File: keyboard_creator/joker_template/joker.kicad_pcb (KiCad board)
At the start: 2 copper layers, 80 x 60 mm, 20 parts, among them U1 BL24C256A-SFRC, U2 STM32F411CEU6, X1 ARM JTAG, Y1 7325-0800A2010-00

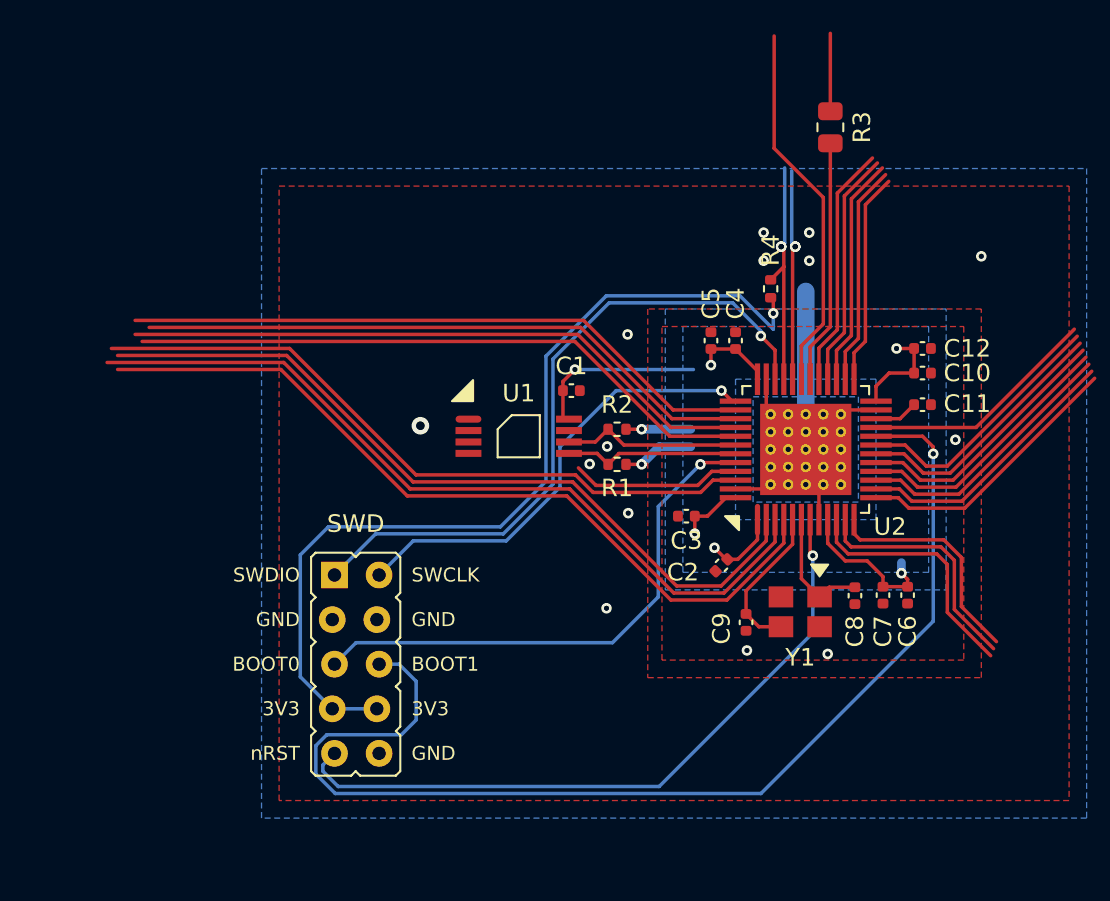
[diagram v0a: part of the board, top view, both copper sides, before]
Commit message: Update joker template to second revision
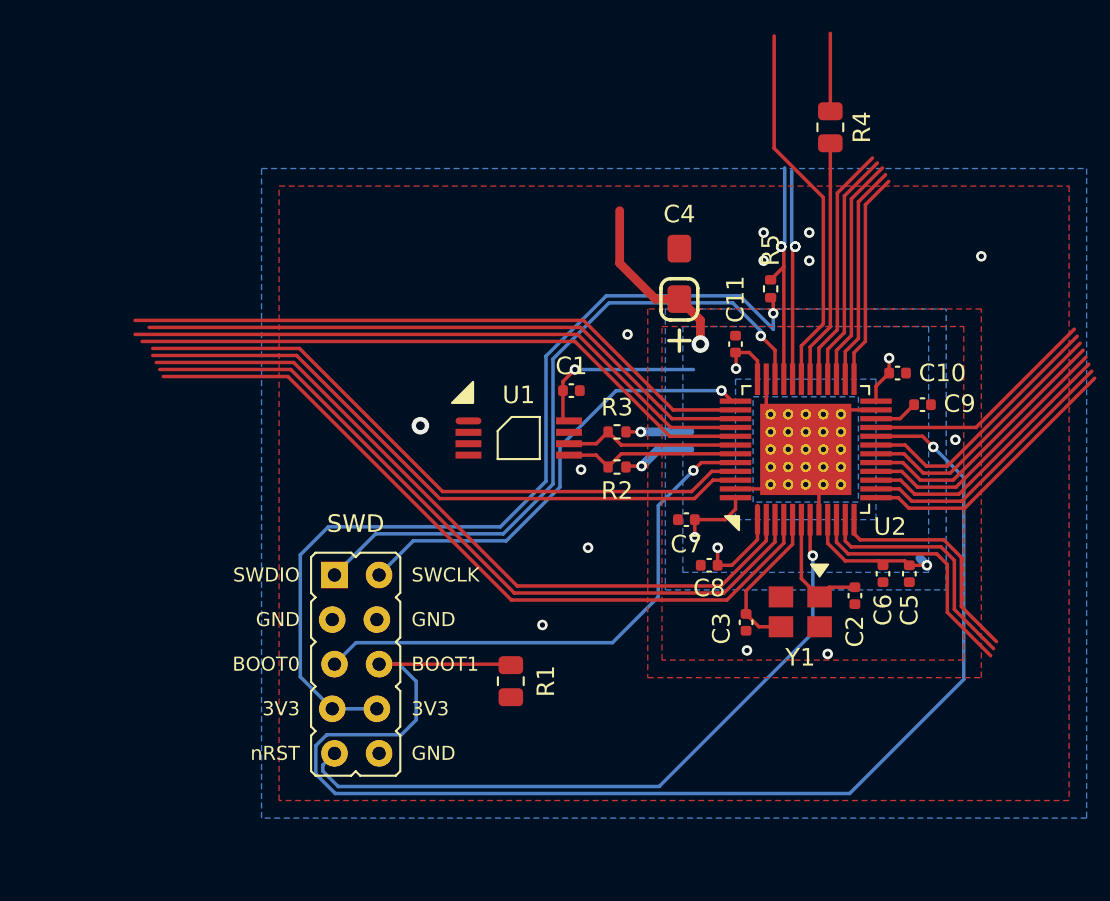
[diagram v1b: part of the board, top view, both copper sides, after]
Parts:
- removed C12: 4.7u, Capacitor_SMD:C_0402_1005Metric
- removed the C5 at (235.3, 118.9)
- added C4: 10u, acheron_Components:CP_EIA-3216-10_Kemet-I_Pad1.58x1.35mm_HandSolder, F.Cu at (233.5, 115.1)
- added R1: 10k, Resistor_SMD:R_0805_2012Metric, F.Cu at (223.9, 138.3)
- C9: renamed from C11; value 2.2u -> 4.7u
- moved C10 1.42 mm to (246.0, 120.8)
- moved C5 1.22 mm to (246.6, 132.2)
- moved C6 1.22 mm to (245.1, 132.2)
- moved C8 0.70 mm to (235.2, 131.7), turned to 180 degrees
- moved C7 0.20 mm to (233.9, 129.1)
- moved C11 0.20 mm to (236.7, 119.1)
- moved R2 0.15 mm to (230.0, 126.1)
- moved R3 0.15 mm to (230.0, 124.1)
- moved U1 0.10 mm to (224.4, 124.5)
- renumbered C4 to C11, C8 to C2, C9 to C3, C6 to C5, C7 to C6, C3 to C7, C2 to C8, R1 to R2, R2 to R3, R3 to R4, R4 to R5
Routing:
- net unconnected-(U2-Pad45): track 9.70 -> 37.1 mm
- net PB2/BOOT1: track 65.8 -> 77.7 mm
- net 3V3: track 96.5 -> 104.1 mm, vias 9 -> 10
- net GND: track 15.2 -> 8.23 mm, vias 14 -> 13
- net unconnected-(U2-Pad3): track 46.0 -> 42.8 mm
- net unconnected-(U2-Pad4): track 46.1 -> 43.3 mm
- net unconnected-(U2-Pad2): track 44.7 -> 42.3 mm
- net unconnected-(U2-Pad46): track 39.2 -> 37.0 mm

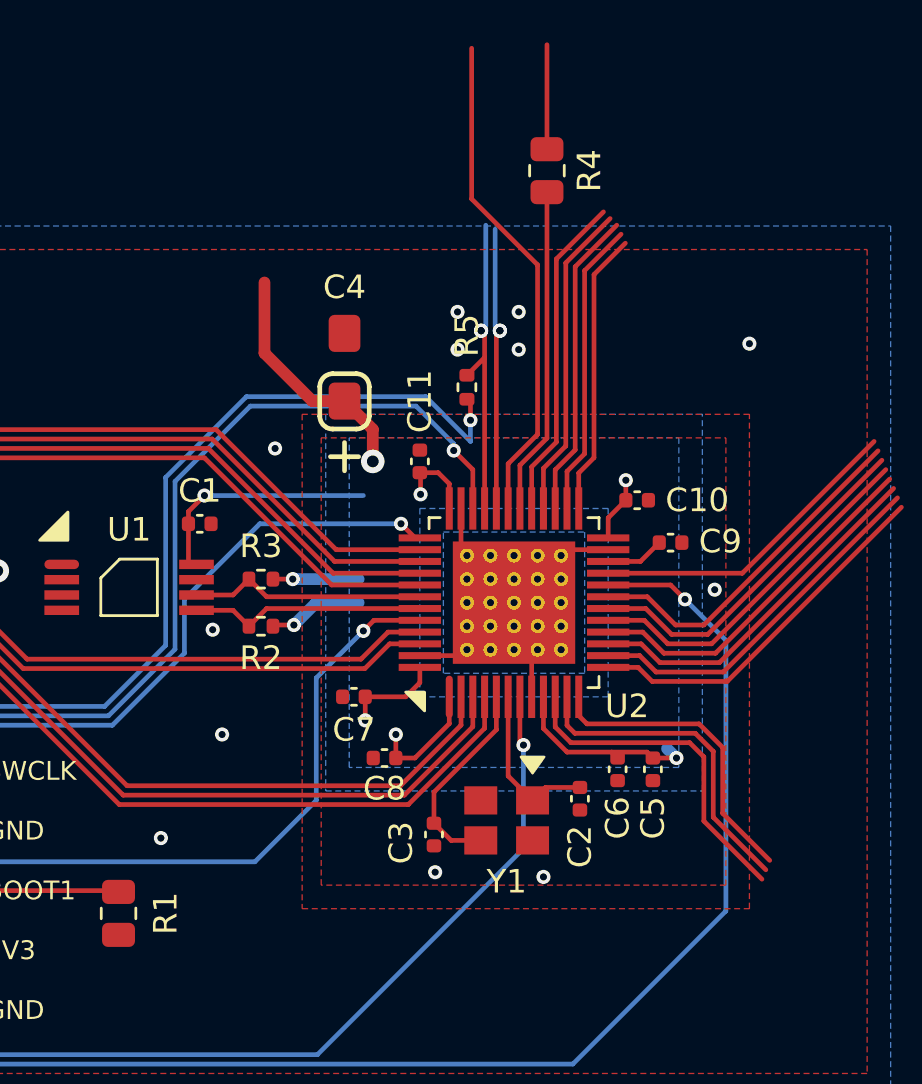
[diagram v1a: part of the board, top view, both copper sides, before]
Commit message: Added KiCAD Dockerfile for building kicad nightly
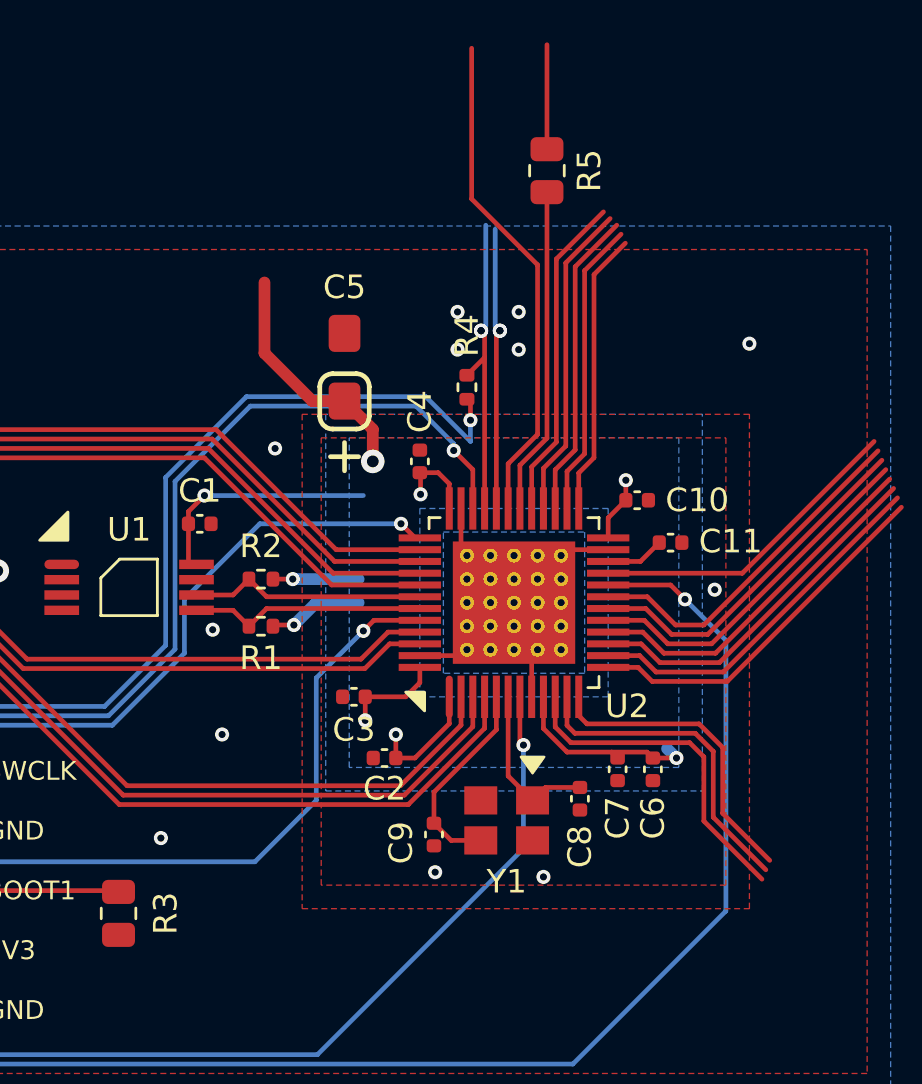
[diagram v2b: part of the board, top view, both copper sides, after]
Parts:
- renumbered C9 to C11, C8 to C2, C7 to C3, C11 to C4, C4 to C5, C5 to C6, C6 to C7, C2 to C8, C3 to C9, R2 to R1, R3 to R2, R1 to R3, R5 to R4, R4 to R5
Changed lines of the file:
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@@
   )
   (net 0 "")
-  (net 1 "Net-(C9-Pad2)")
+  (net 1 "Net-(C11-Pad2)")
   (net 2 "GND")
   (net 3 "3V3")
@@
     (property "Sheetname" "")
     (attr smd)
-    (fp_text reference "C3" (at 0.35 1.4 90) (layer "F.SilkS")
+    (fp_text reference "C9" (at 0.35 1.4 90) (layer "F.SilkS")
       (effects (font (size 1 1) (thickness 0.2)))
     )
@@
     (property "Sheetname" "")
     (attr smd)
-    (fp_text reference "C9" (at -1.2 0.05) (layer "F.SilkS")
+    (fp_text reference "C11" (at -1.2 0.05) (layer "F.SilkS")
       (effects (font (size 1 1) (thickness 0.2)) (justify left))
     )
@@
       (net 2 "GND") (pintype "passive"))
     (pad "2" smd roundrect locked (at 0.48 0 180) (size 0.56 0.62) (layers "F.Cu" "F.Paste" "F.Mask") (roundrect_rratio 0.25)
-      (net 1 "Net-(C9-Pad2)") (pintype "passive"))
+      (net 1 "Net-(C11-Pad2)") (pintype "passive"))
     (model "${KICAD6_3DMODEL_DIR}/Capacitor_SMD.3dshapes/C_0402_1005Metric.wrl"
       (offset (xyz 0 0 0))
@@
     (property "Sheetname" "")
     (attr smd)
-    (fp_text reference "R4" (at 0 -1.8 90) (layer "F.SilkS")
+    (fp_text reference "R5" (at 0 -1.8 90) (layer "F.SilkS")
       (effects (font (size 1 1) (thickness 0.2)))
     )
@@
       (net 26 "unconnected-(U2-Pad21)") (pinfunction "B10") (pintype "bidirectional"))
     (pad "22" smd rect locked (at 1.75 4 180) (size 1.8 0.3) (layers "F.Cu" "F.Paste" "F.Mask")
-      (net 1 "Net-(C9-Pad2)") (pinfunction "VCAP_1") (pintype "output"))
+      (net 1 "Net-(C11-Pad2)") (pinfunction "VCAP_1") (pintype "output"))
     (pad "23" smd rect locked (at 2.25 4 180) (size 1.8 0.3) (layers "F.Cu" "F.Paste" "F.Mask")
       (net 2 "GND") (pinfunction "VSS") (pintype "power_out"))
@@
     (property "Specification" "MLCC 10V or more")
     (attr smd)
-    (fp_text reference "C8" (at 0 -1.3 180) (layer "F.SilkS")
+    (fp_text reference "C2" (at 0 -1.3 180) (layer "F.SilkS")
       (effects (font (size 1 1) (thickness 0.2)))
     )
@@
     (property "Sheetname" "")
     (attr smd)
-    (fp_text reference "C4" (at 3.4 0 180) (layer "F.SilkS")
+    (fp_text reference "C5" (at 3.4 0 180) (layer "F.SilkS")
       (effects (font (size 1 1) (thickness 0.2)))
     )
@@
     (property "Specification" "MLCC 10V or more")
     (attr smd)
-    (fp_text reference "C5" (at 1.15 0 90) (layer "F.SilkS")
+    (fp_text reference "C6" (at 1.15 0 90) (layer "F.SilkS")
       (effects (font (size 1 1) (thickness 0.2)) (justify right))
     )
@@
     (property "Specification" "MLCC 10V or more")
     (attr smd)
-    (fp_text reference "C7" (at 0 -1.4) (layer "F.SilkS")
+    (fp_text reference "C3" (at 0 -1.4) (layer "F.SilkS")
       (effects (font (size 1 1) (thickness 0.2)))
     )
@@
     (property "Sheetname" "")
     (attr smd)
-    (fp_text reference "C2" (at 1.12 0 90) (layer "F.SilkS")
+    (fp_text reference "C8" (at 1.12 0 90) (layer "F.SilkS")
       (effects (font (size 1 1) (thickness 0.2)) (justify right))
     )
@@
     (property "Sheetname" "")
     (attr smd)
-    (fp_text reference "R2" (at 0 -1.35) (layer "F.SilkS")
+    (fp_text reference "R1" (at 0 -1.35) (layer "F.SilkS")
       (effects (font (size 1 1) (thickness 0.2)))
     )
@@
     (property "Sheetname" "")
     (attr smd)
-    (fp_text reference "R5" (at 2.2 0 90) (layer "F.SilkS")
+    (fp_text reference "R4" (at 2.2 0 90) (layer "F.SilkS")
       (effects (font (size 1 1) (thickness 0.2)))
     )
@@
     (property "Sheetname" "")
     (attr smd)
-    (fp_text reference "R3" (at 0 1.4) (layer "F.SilkS")
+    (fp_text reference "R2" (at 0 1.4) (layer "F.SilkS")
       (effects (font (size 1 1) (thickness 0.2)))
     )
@@
     (property "Sheetname" "")
     (attr smd)
-    (fp_text reference "R1" (at 0 -2 90) (layer "F.SilkS")
+    (fp_text reference "R3" (at 0 -2 90) (layer "F.SilkS")
       (effects (font (size 1 1) (thickness 0.2)))
     )
@@
     (property "Specification" "MLCC 10V or more")
     (attr smd)
-    (fp_text reference "C11" (at -1.2 0 90) (layer "F.SilkS")
+    (fp_text reference "C4" (at -1.2 0 90) (layer "F.SilkS")
       (effects (font (size 1 1) (thickness 0.2)) (justify left))
     )
@@
     (property "Specification" "MLCC 10V or more")
     (attr smd)
-    (fp_text reference "C6" (at 1.15 0 90) (layer "F.SilkS")
+    (fp_text reference "C7" (at 1.15 0 90) (layer "F.SilkS")
       (effects (font (size 1 1) (thickness 0.2)) (justify right))
     )
